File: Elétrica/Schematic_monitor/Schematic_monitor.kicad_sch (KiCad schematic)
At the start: 49 parts, among them J1 Conn_01x04, J2 USB_B_Micro, J3 Eletrode 1, J4 Eletrode 2, SW1 SW_Push, SW2 SW_SPDT, U1 STM32F446RET6TR, U2 LM1117S-3.3, U3 MLX90614ESF-ACC-000-TU, U4 MAX30100EFD+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

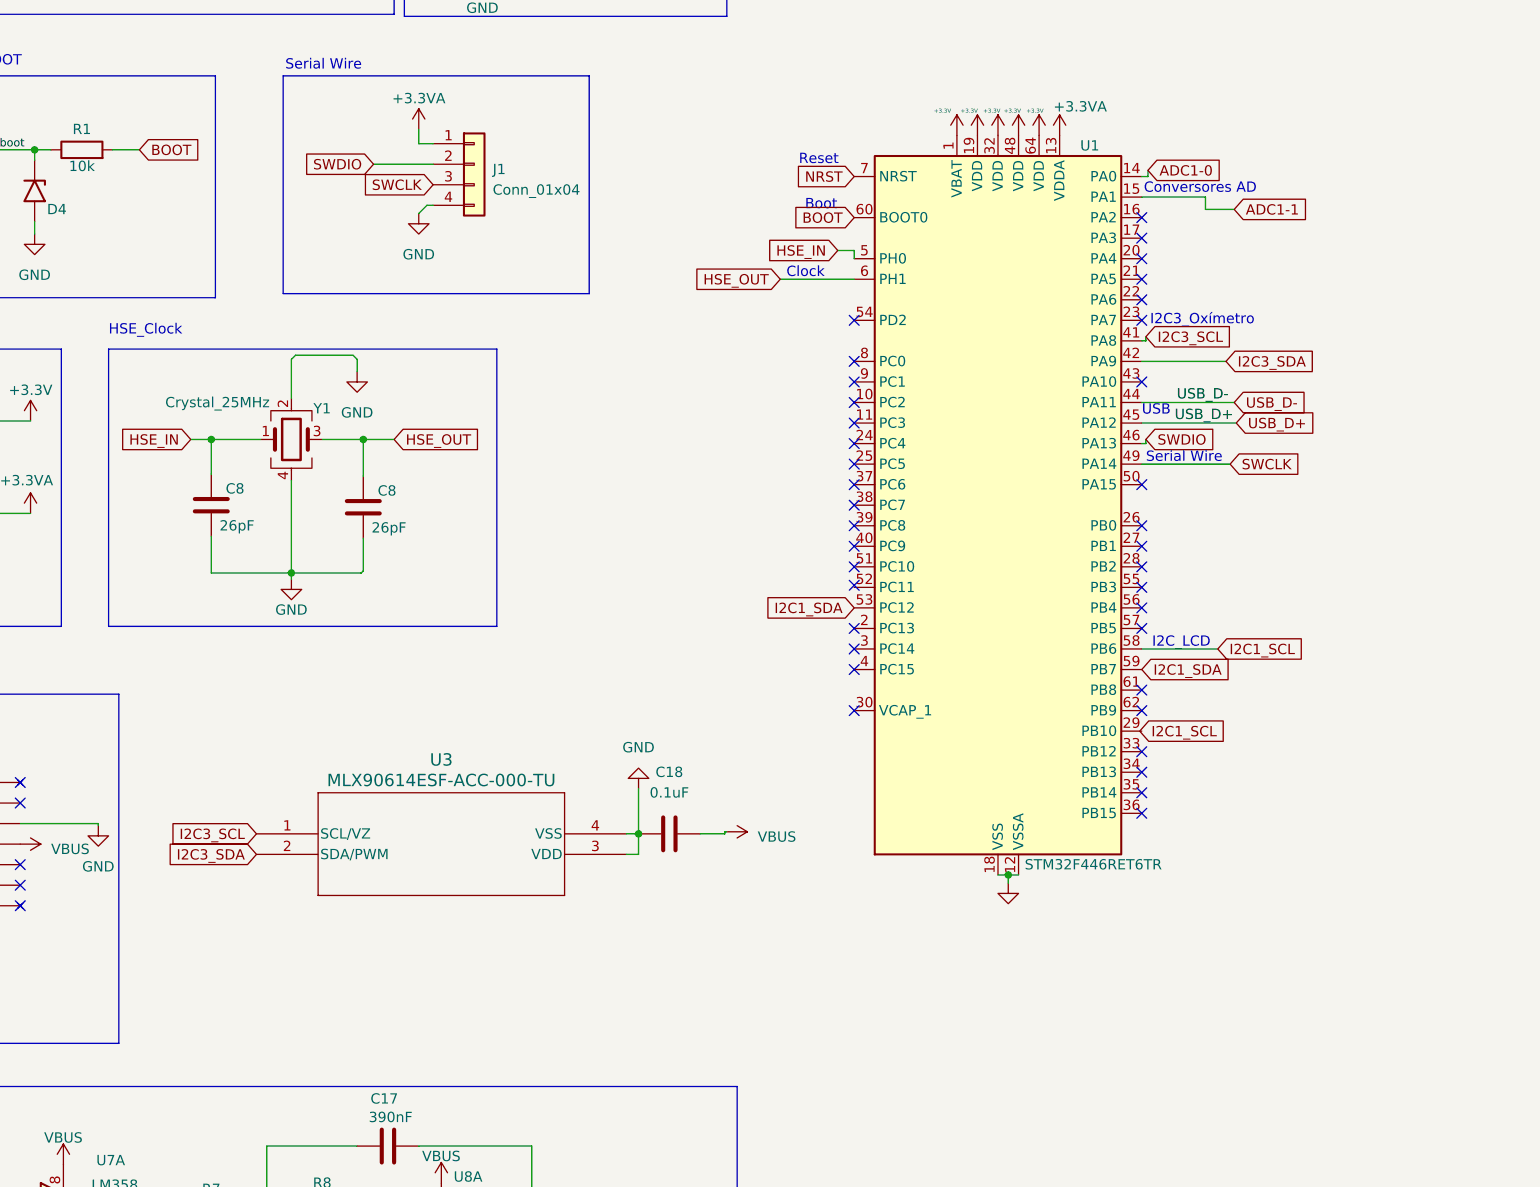
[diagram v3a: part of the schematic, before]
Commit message: kicad labels
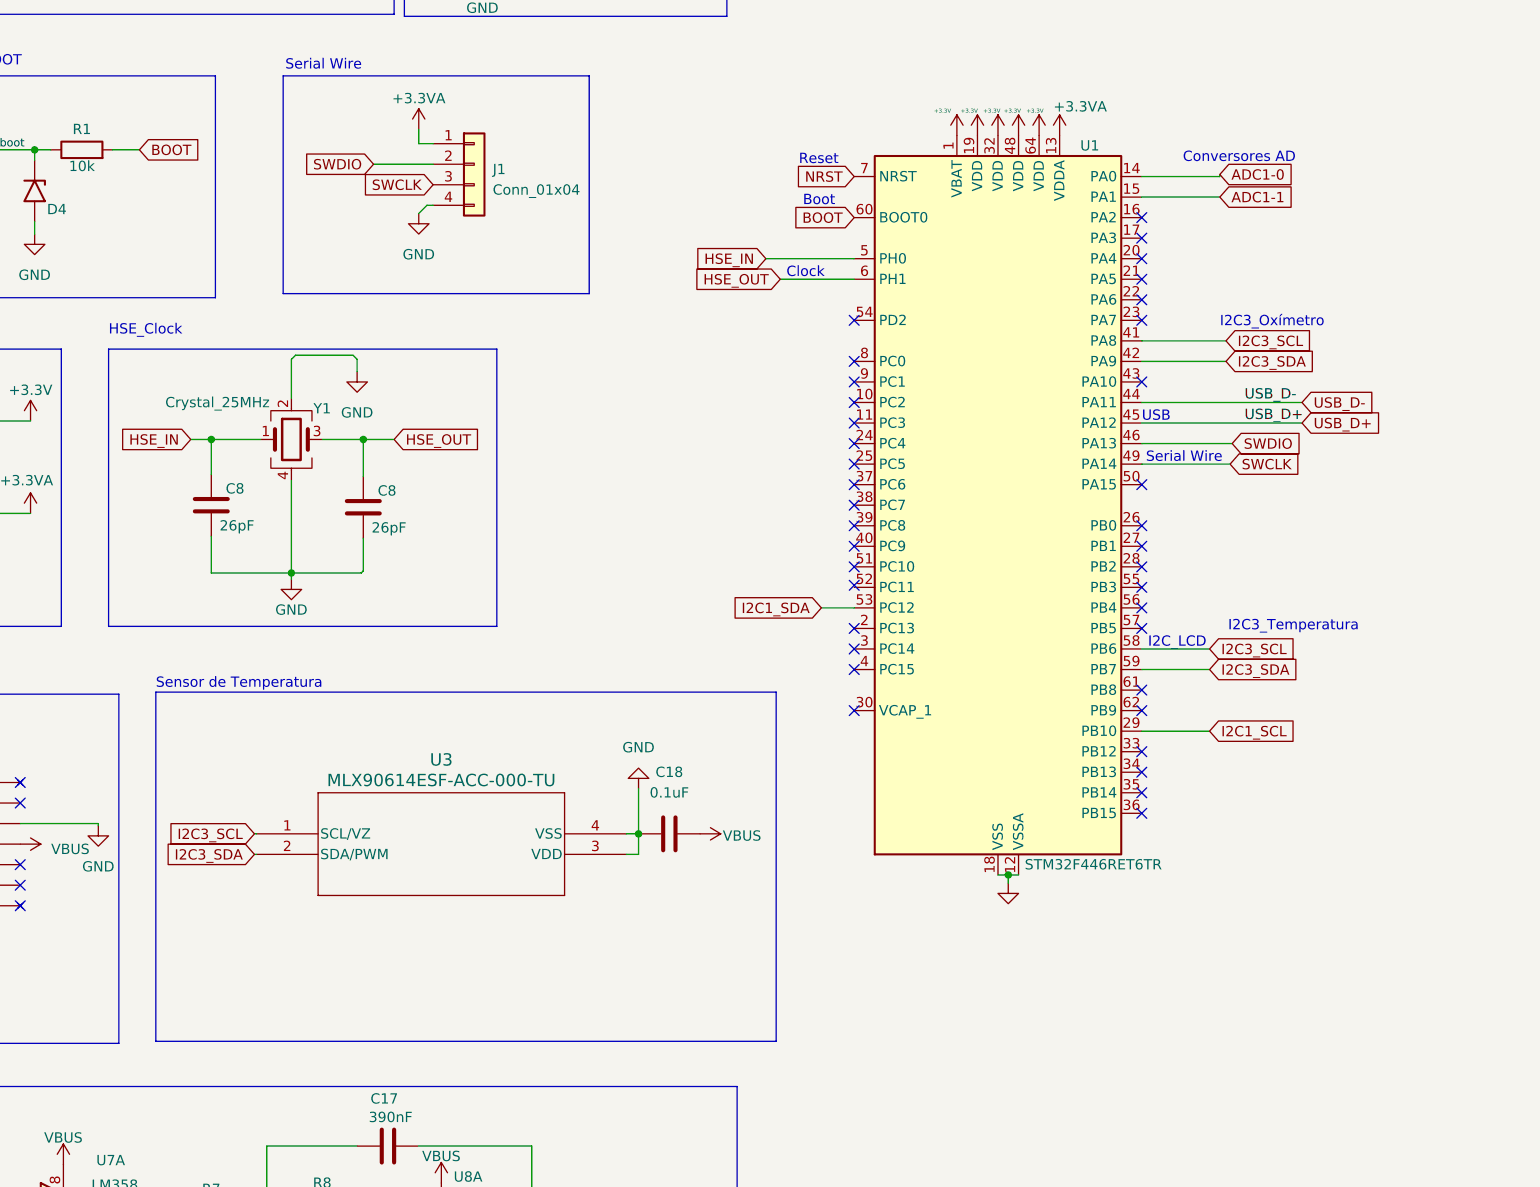
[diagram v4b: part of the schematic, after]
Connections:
- net I2C1_SCL: now also U1.29 (PB10); no longer U1.58 (PB6)
- net I2C1_SDA: no longer U1.59 (PB7)
- net I2C3_SCL: now also U1.58 (PB6)
- net I2C3_SDA: now also U1.59 (PB7)
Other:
- note added: "I2C3_Temperatura"
- note added: "Sensor de Temperatura"

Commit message: Atualizações
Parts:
- J3, J4: footprint Connector_PinHeader_1.00mm:PinHeader_1x01_P1.00mm_Horizontal -> Connector_PinHeader_2.54mm:PinHeader_1x01_P2.54mm_Vertical
- U3: footprint MLX90614xCC_MEL -> temp:MLX90614xCC_MEL
- U4: footprint oxy:21-0880B_MXM -> oximeter:21-0880B_MXM-L
- U5: footprint (none) -> AD623:RM_8_ADI-L
- U6, U7, U8: footprint (none) -> LM358:D8-L
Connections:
- net GND: now also C18.1; no longer C18.2, U3.3 (VDD)
- net VBUS: now also C18.2, U3.3 (VDD); no longer C18.1
- net EMG: now reaches J3.1 (Pin_1), U5.2 (-)
- net I2C1_SCL renamed Temp_SCL
- net Temp_SCL: now also U3.1 (SCL/VZ)
- net I2C1_SDA renamed Temp_SDA
- net Temp_SDA: now also U3.2 (SDA/PWM)
- net I2C3_SCL renamed oxi_scl
- net oxi_scl: no longer U1.58 (PB6), U3.1 (SCL/VZ)
- net I2C3_SDA renamed oxi_sda
- net oxi_sda: no longer U1.59 (PB7), U3.2 (SDA/PWM)
- new net scl_lcd: U1.58 (PB6)
- new net sda_lcd: U1.59 (PB7)
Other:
- note added: "I2C2_Temperatura"
- note added: "I2C3_LCD"
- note removed: "I2C3_Temperatura"
- note removed: "I2C_LCD"
- moved on the sheet: C18
